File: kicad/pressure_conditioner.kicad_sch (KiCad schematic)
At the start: 8 parts, among them J1 5023520201, J2 5023520201, J3 5023520201, J4 5023520201, J5 5023520201, J6 5023520201, J7 5023520201

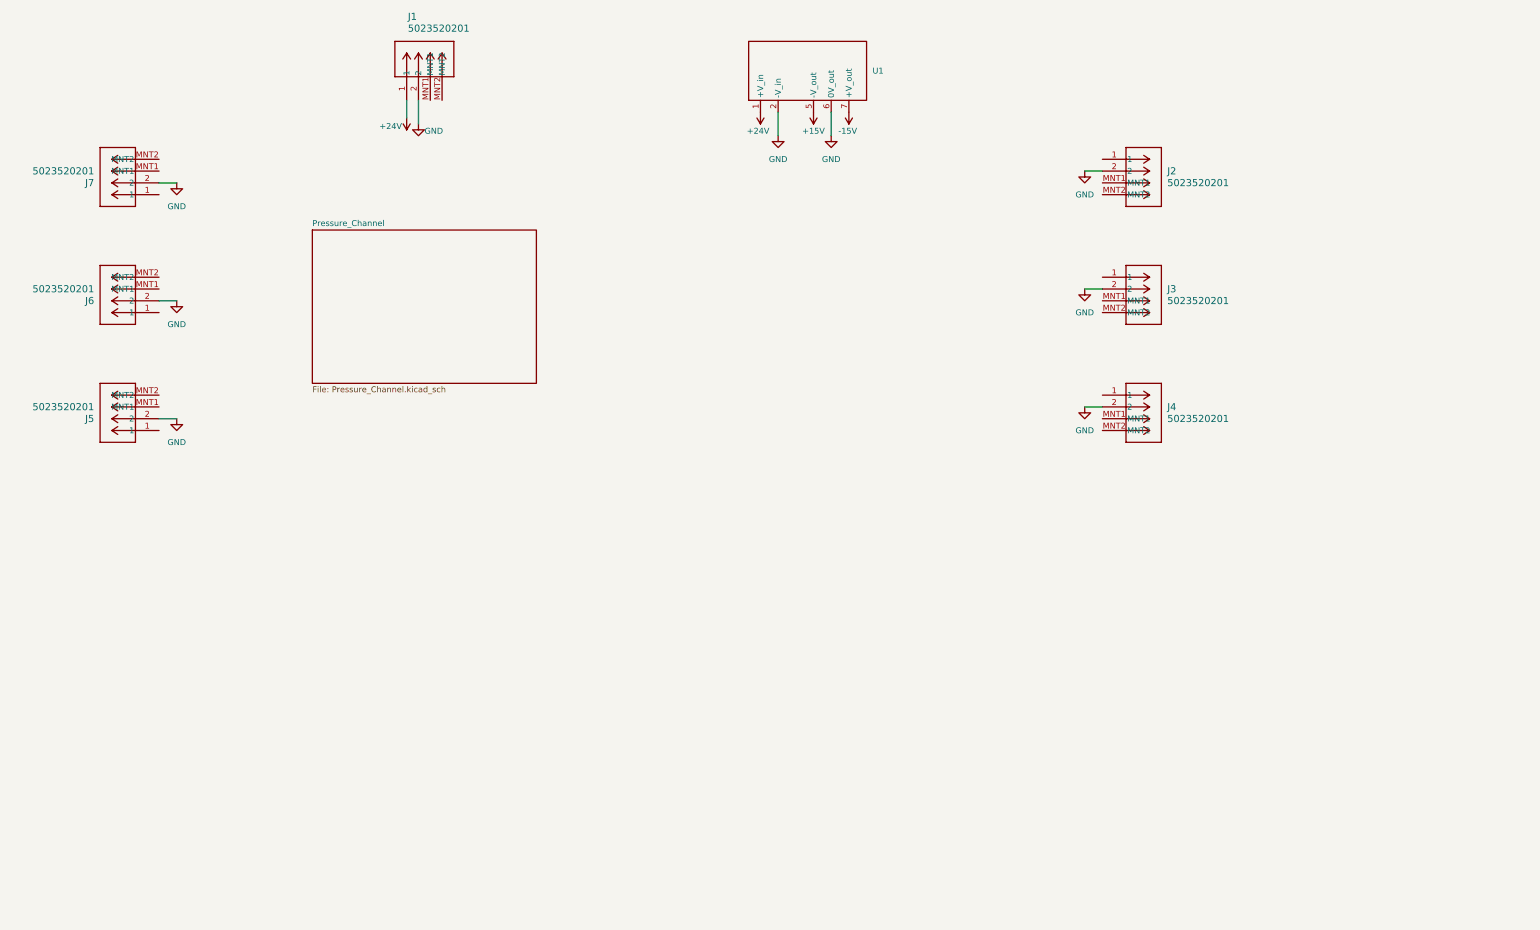
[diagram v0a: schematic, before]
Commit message: finished RCV420 channel sheet with capacitors for smoothing, reistor for protection, options TVS, and labels, now working on top sheet connections
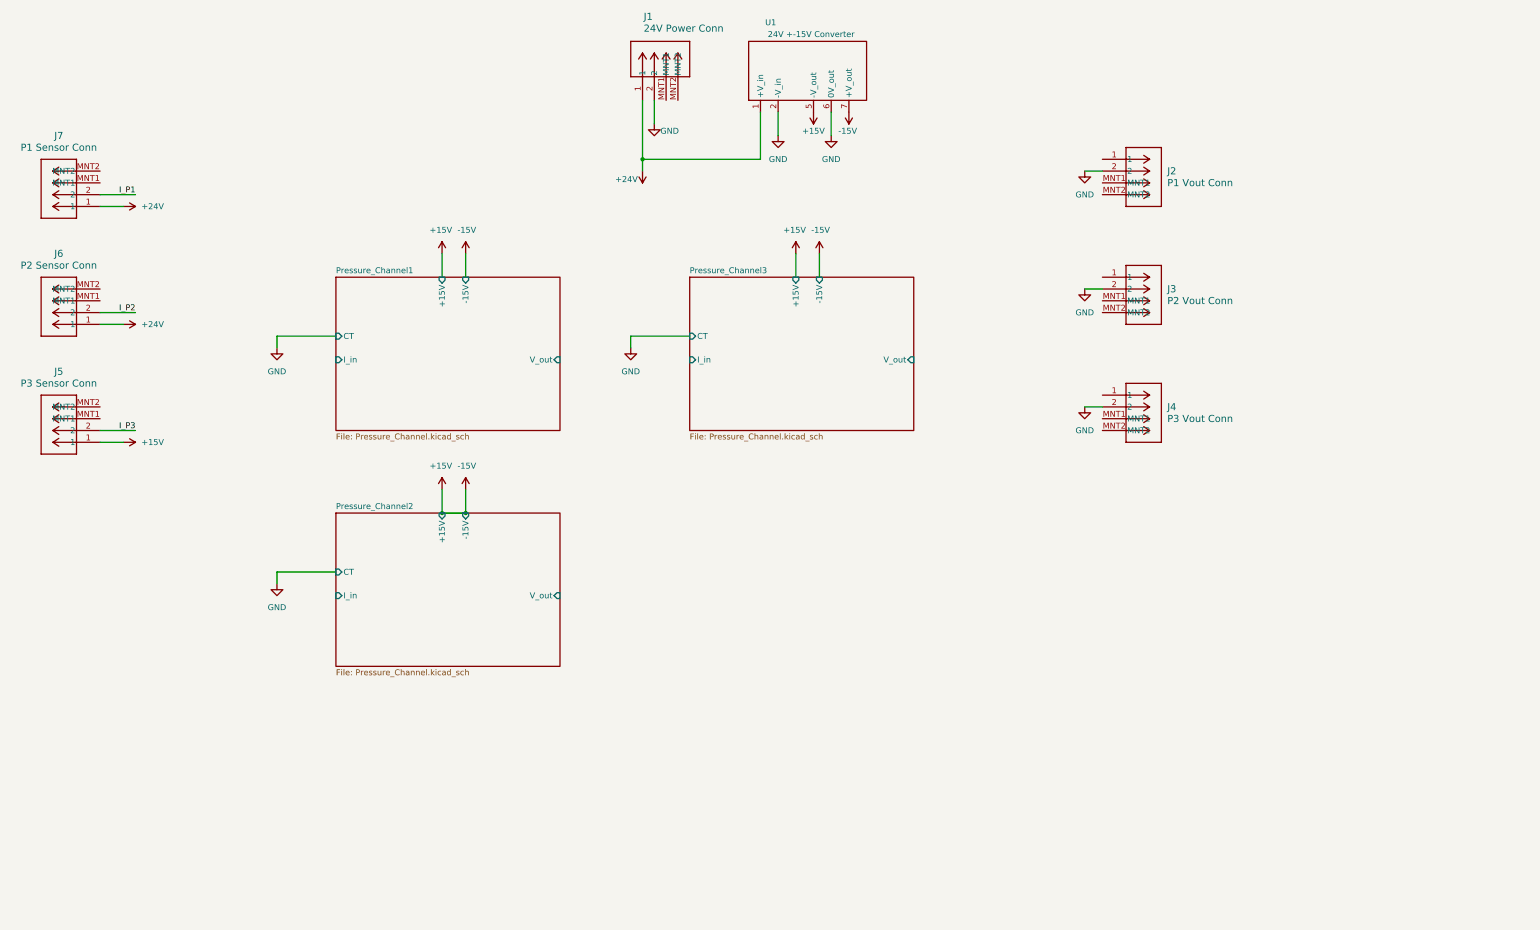
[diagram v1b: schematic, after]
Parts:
- J1: value 5023520201 -> 24V Power Conn
- J2: value 5023520201 -> P1 Vout Conn
- J3: value 5023520201 -> P2 Vout Conn
- J4: value 5023520201 -> P3 Vout Conn
- J5: value 5023520201 -> P3 Sensor Conn
- J6: value 5023520201 -> P2 Sensor Conn
- J7: value 5023520201 -> P1 Sensor Conn
- U1: value (none) -> 24V +-15V Converter
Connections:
- net -15V is gone; now on net +15V: U1.7 (+V_out)
- net +15V: now also J5.1
- net +24V: now also J6.1, J7.1
- net GND: no longer J5.2, J6.2, J7.2
- new net I_P1: J7.2
- new net I_P2: J6.2
- new net I_P3: J5.2
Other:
- sheet Pressure_Channel renamed Pressure_Channel1
- added sheet Pressure_Channel2 (Pressure_Channel.kicad_sch)
- added sheet Pressure_Channel3 (Pressure_Channel.kicad_sch)
- sheet Pressure_Channel1 ports: added +15V, -15V, CT, I_in, V_out; removed none
- company: (none) -> JRPD
- title: (none) -> Three Channel Pressure Signal Conditioner
- moved on the sheet: J1, J5, J6, J7

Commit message: began pcb layout
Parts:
- J1, J2, J3, J4, J5, J6, J7: footprint CONN_SD-502352-001_02_MOL -> Pressure:MOLEX_5023520201_2_Wire_DuraClik
- U1: footprint CONN_SD-502352-001_02_MOL -> Pressure:Murata_24-+-15_Conv_NMK2415SC
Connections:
- net +15V: no longer J5.1
- net +24V: now also J5.1
- net Vout_P1: now reaches J2.1
- net Vout_P2: now reaches J4.1
- net Vout_P2: now also J3.1

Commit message: Finished preliminary layout of Rev. A of board
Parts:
- removed U1: 24V +-15V Converter, Pressure:Murata_24-+-15_Conv_NMK2415SC, symbol Pressure:NMK2415SAC
- added PS1: NMK2415SC, Pressure:Murata_24-+-15_Conv_NMK2415SC, symbol Pressure:NMK2415SC
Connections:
- net +15V: now also PS1.7 (+VOUT)
- net +24V: now also PS1.1 (+VIN)
- net GND: now also PS1.2 (-VIN), PS1.6 (OV)
- net Vout_P2: no longer J4.1
- net Vout_P3: now also J4.1
- new net -15V: PS1.5 (-VOUT)
- no-connect marks 0 -> 14

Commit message: visual changes, nothing structural
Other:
- moved on the sheet: J1, J2, J3, J4, J5, J6, J7, PS1
